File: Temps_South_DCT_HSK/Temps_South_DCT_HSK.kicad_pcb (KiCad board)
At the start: 2 copper layers, 53.3 x 63.5 mm, 9 parts, among them J1 North_Temps_1, J2 North_Temps_2, J3 Internal_Temps_DCT_HSK_Box_1, J4 Internal_Temps_DCT_HSK_Box_2

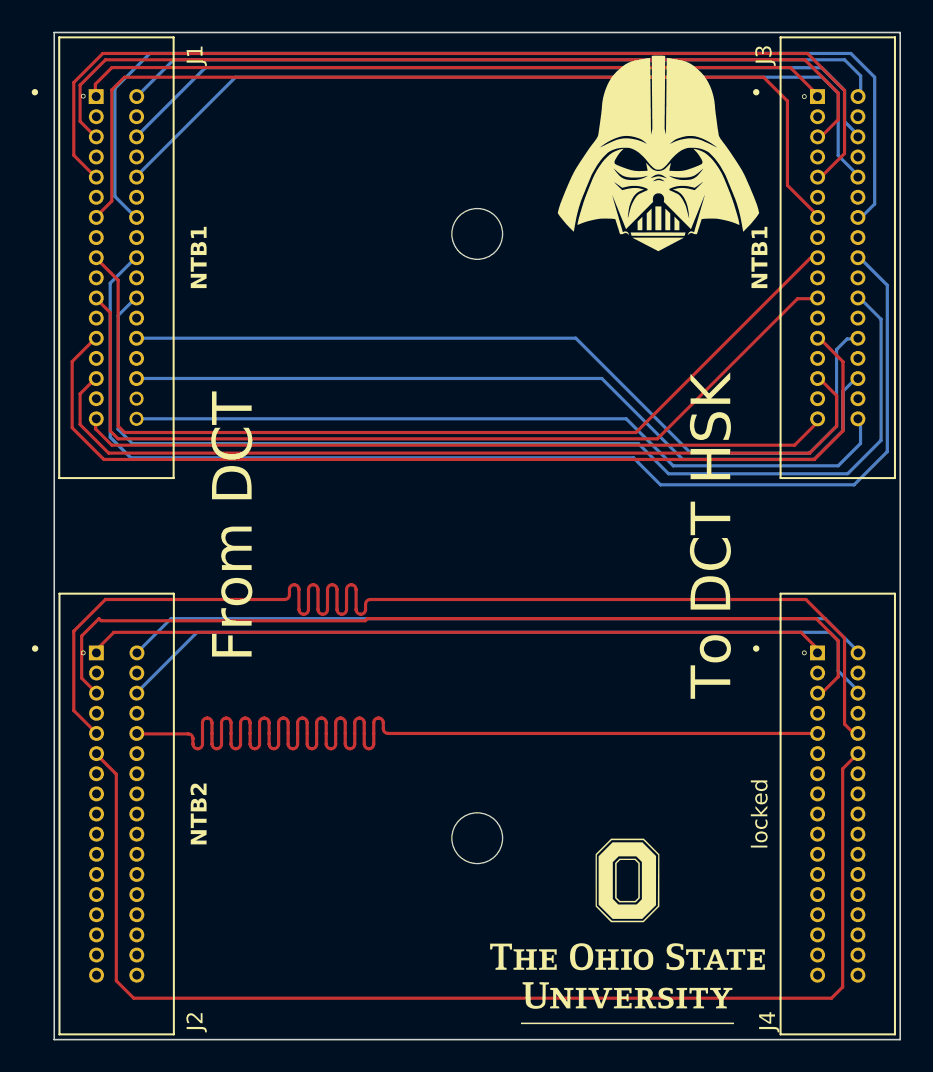
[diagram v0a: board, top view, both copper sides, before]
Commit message: Updated Heater and Temp PCBs to board size 2.5in x 2.1in. Updated traces and silkscreens
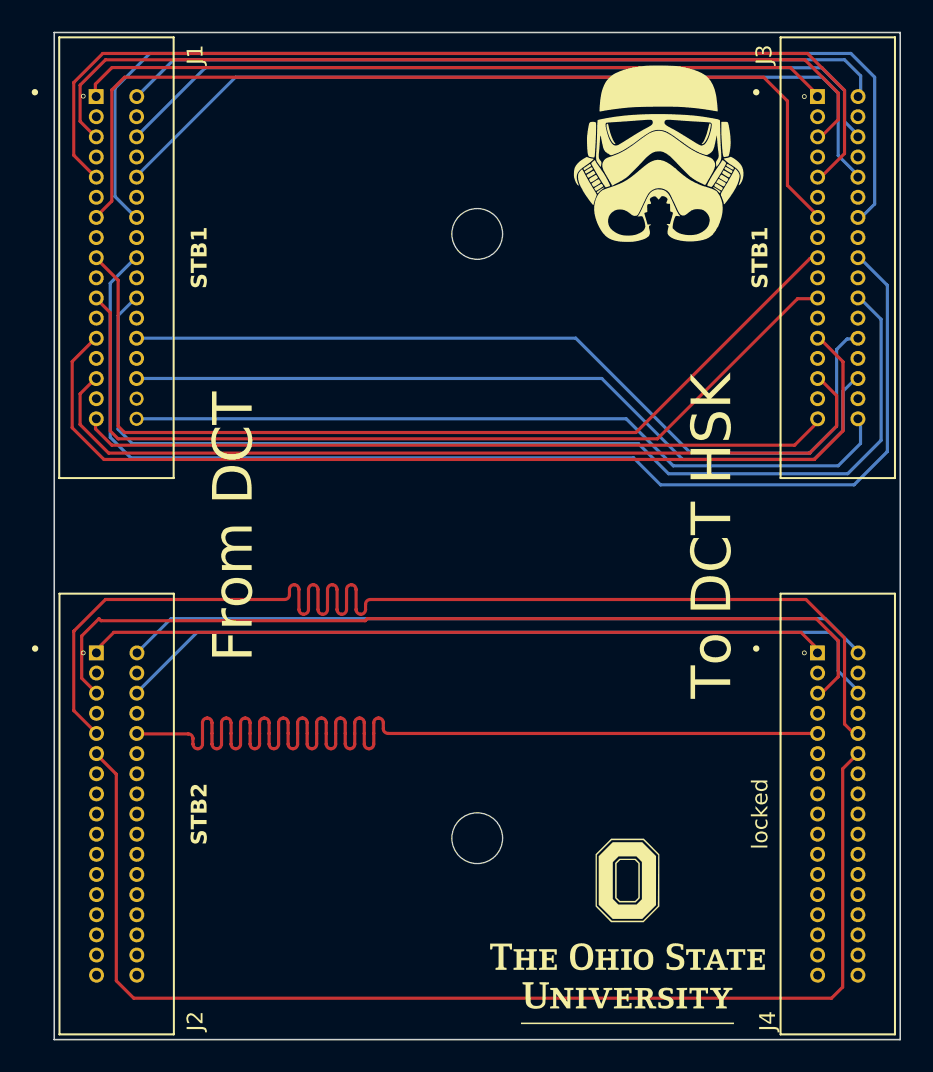
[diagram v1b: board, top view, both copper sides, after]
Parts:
- G***: value LOGO -> Stormtrooper; footprint LOGO -> Fun_Logos:Stormtrooper
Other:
- board text added: "STB1"
- board text added: "STB2"
- board text added: "South"
- board text added: "Temps South Rev B Dennis H. Calderon 09/09/2023"
- board text removed: "NTB1"
- board text removed: "NTB2"
- board text removed: "North"
- board text removed: "Temps North Rev B Dennis H. Calderon 09/09/2023"

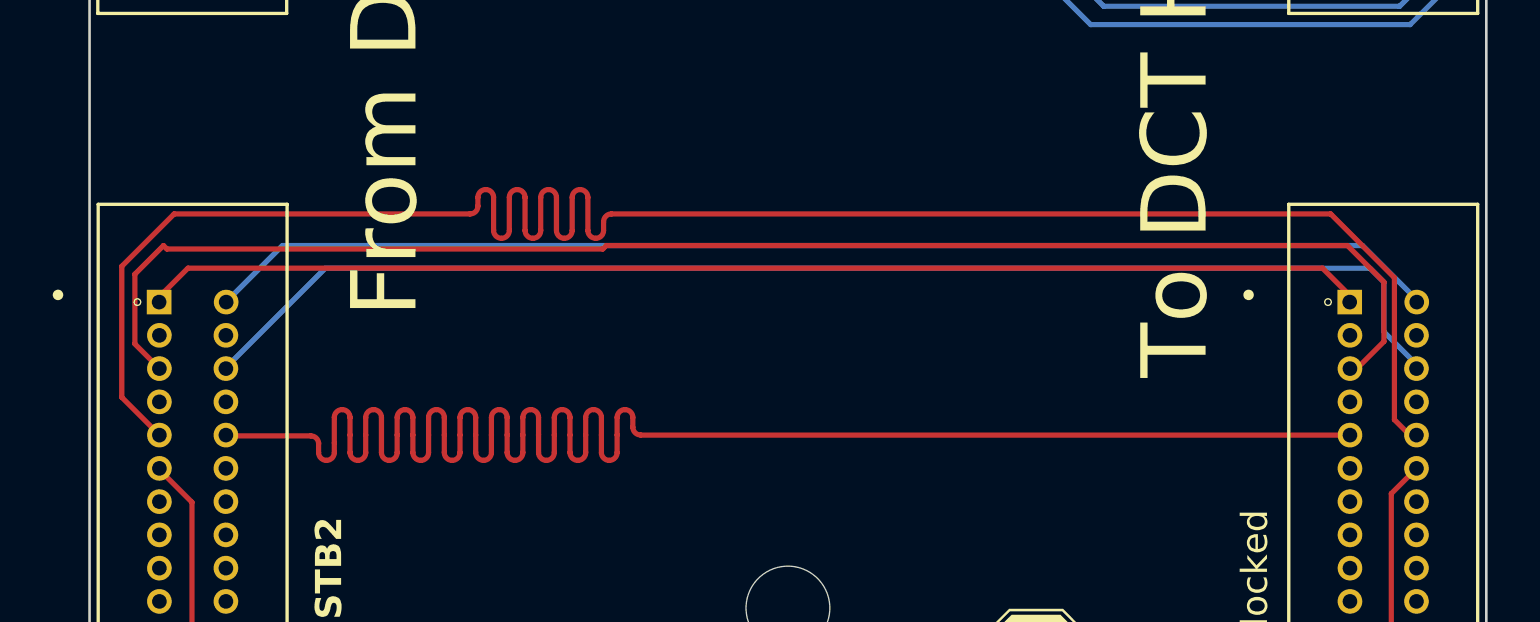
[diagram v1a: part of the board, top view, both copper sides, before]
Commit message: Tuned RTD tracks for Temp boards
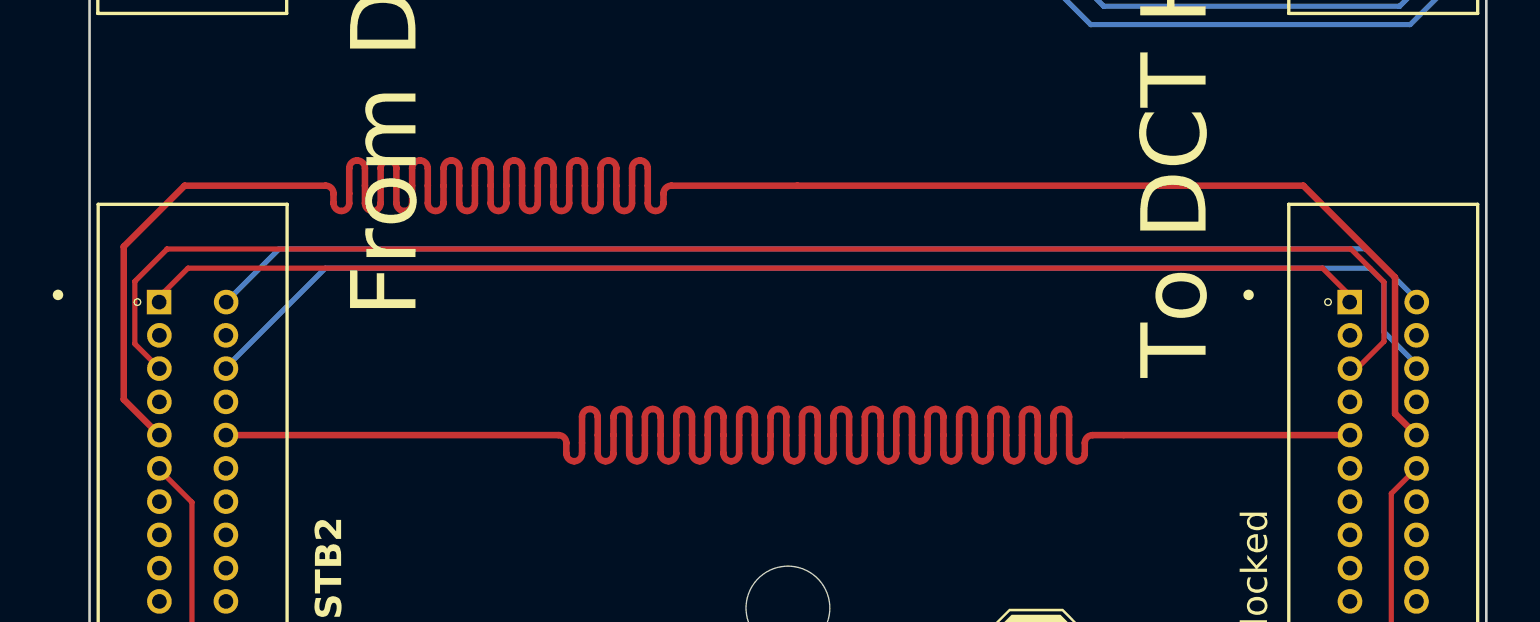
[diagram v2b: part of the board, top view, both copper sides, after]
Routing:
- net /TD2_10: track 75.7 -> 99.2 mm
- net /TD2_9: track 76.6 -> 99.5 mm

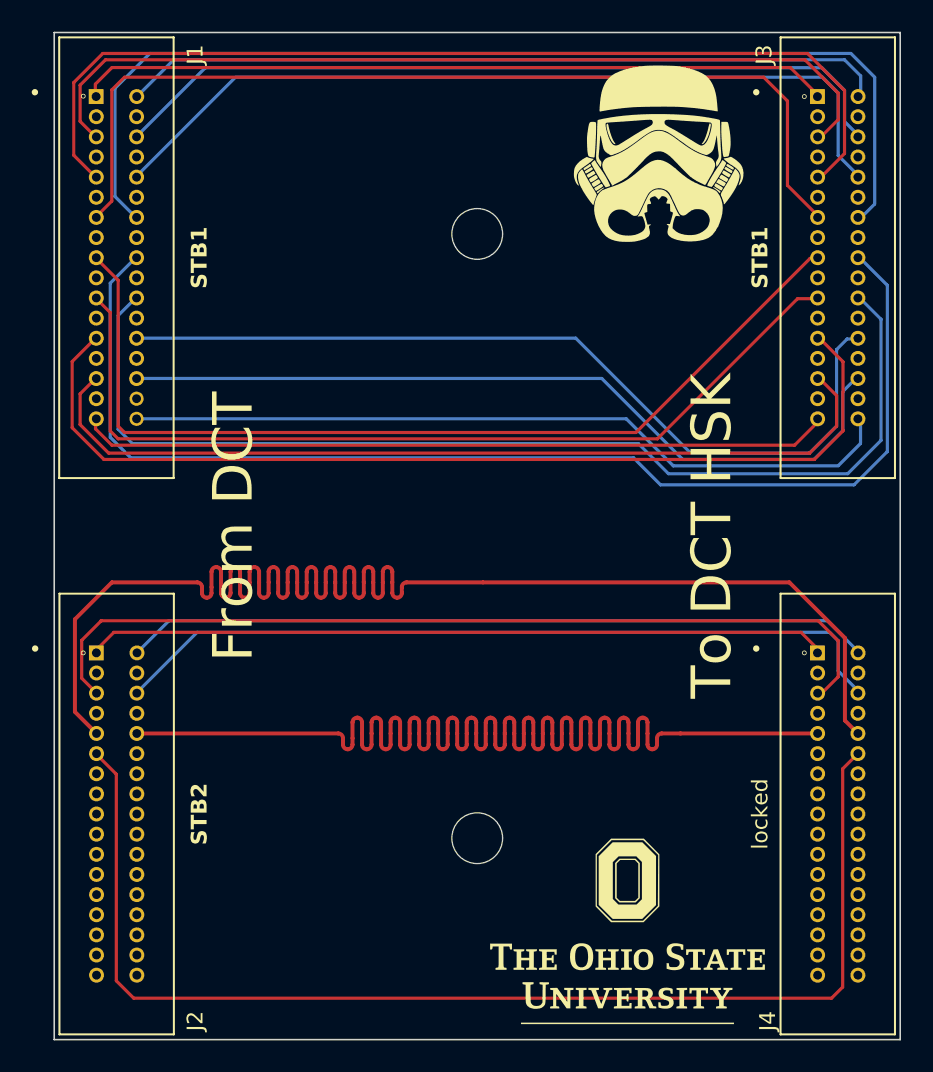
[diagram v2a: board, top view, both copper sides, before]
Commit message: Tuned RTD tracks on Temp boards
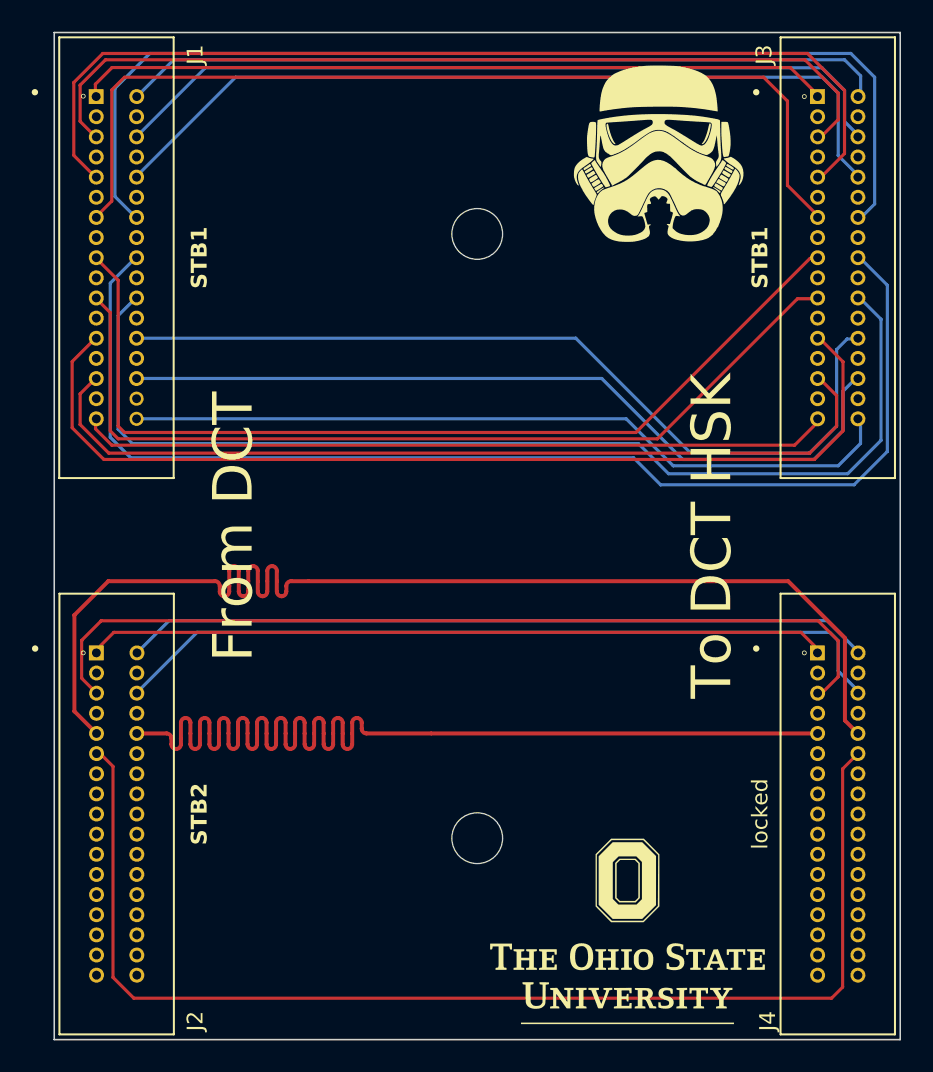
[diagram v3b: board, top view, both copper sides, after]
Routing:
- net /TD2_10: track 99.2 -> 76.1 mm
- net /TD2_9: track 99.5 -> 76.4 mm
